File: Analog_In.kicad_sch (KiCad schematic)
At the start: 16 parts, among them J301 Piezos, U301 TL082, U302 TL082, U303 ADS1115IDGS

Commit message: Switch ADC
Switched from the ADS1115 to ADS7924 to get faster sampling time.
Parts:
- removed U303: ADS1115IDGS, Package_SO:TSSOP-10_3x3mm_P0.5mm, symbol Analog_ADC:ADS1115IDGS
- added C305, C306: 1u, Capacitor_SMD:C_0402_1005Metric, symbol Device:C_Small
- added U303: ADS7924, Package_DFN_QFN:WQFN-16-1EP_3x3mm_P0.5mm_EP1.68x1.68mm, symbol Analog_ADC:ADS7924
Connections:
- net +5VA: now also C306.1, U303.15 (AVDD)
- net ADC_AIN0: now also U303.12 (CH0)
- net ADC_AIN1: now also U303.11 (CH1)
- net ADC_AIN2: now also U303.10 (CH2)
- net ADC_AIN3: now also U303.9 (CH3)
- net AIN0: now also J301.2 (Pin_2); no longer J301.8 (Pin_8)
- net AIN1: now also J301.4 (Pin_4); no longer J301.6 (Pin_6)
- net AIN2: now also J301.6 (Pin_6); no longer J301.4 (Pin_4)
- net AIN3: now also J301.8 (Pin_8); no longer J301.2 (Pin_2)
- net GND: now also C305.2, C306.2, U303.17 (pad), U303.5 (A0), U303.6 (DGND), U303.8 (AGND)
- net MCU_ADC_INT: now also U303.2 (~{INT})
- net MCU_SCL: now also U303.3 (SCLK)
- net MCU_SDA: now also U303.4 (SDA)
- new net: U303.13 (MUXOUT), U303.14 (ADCIN)
- new net +3.3V: C305.1, U303.16 (DVDD)
- no-connect marks 0 -> 2

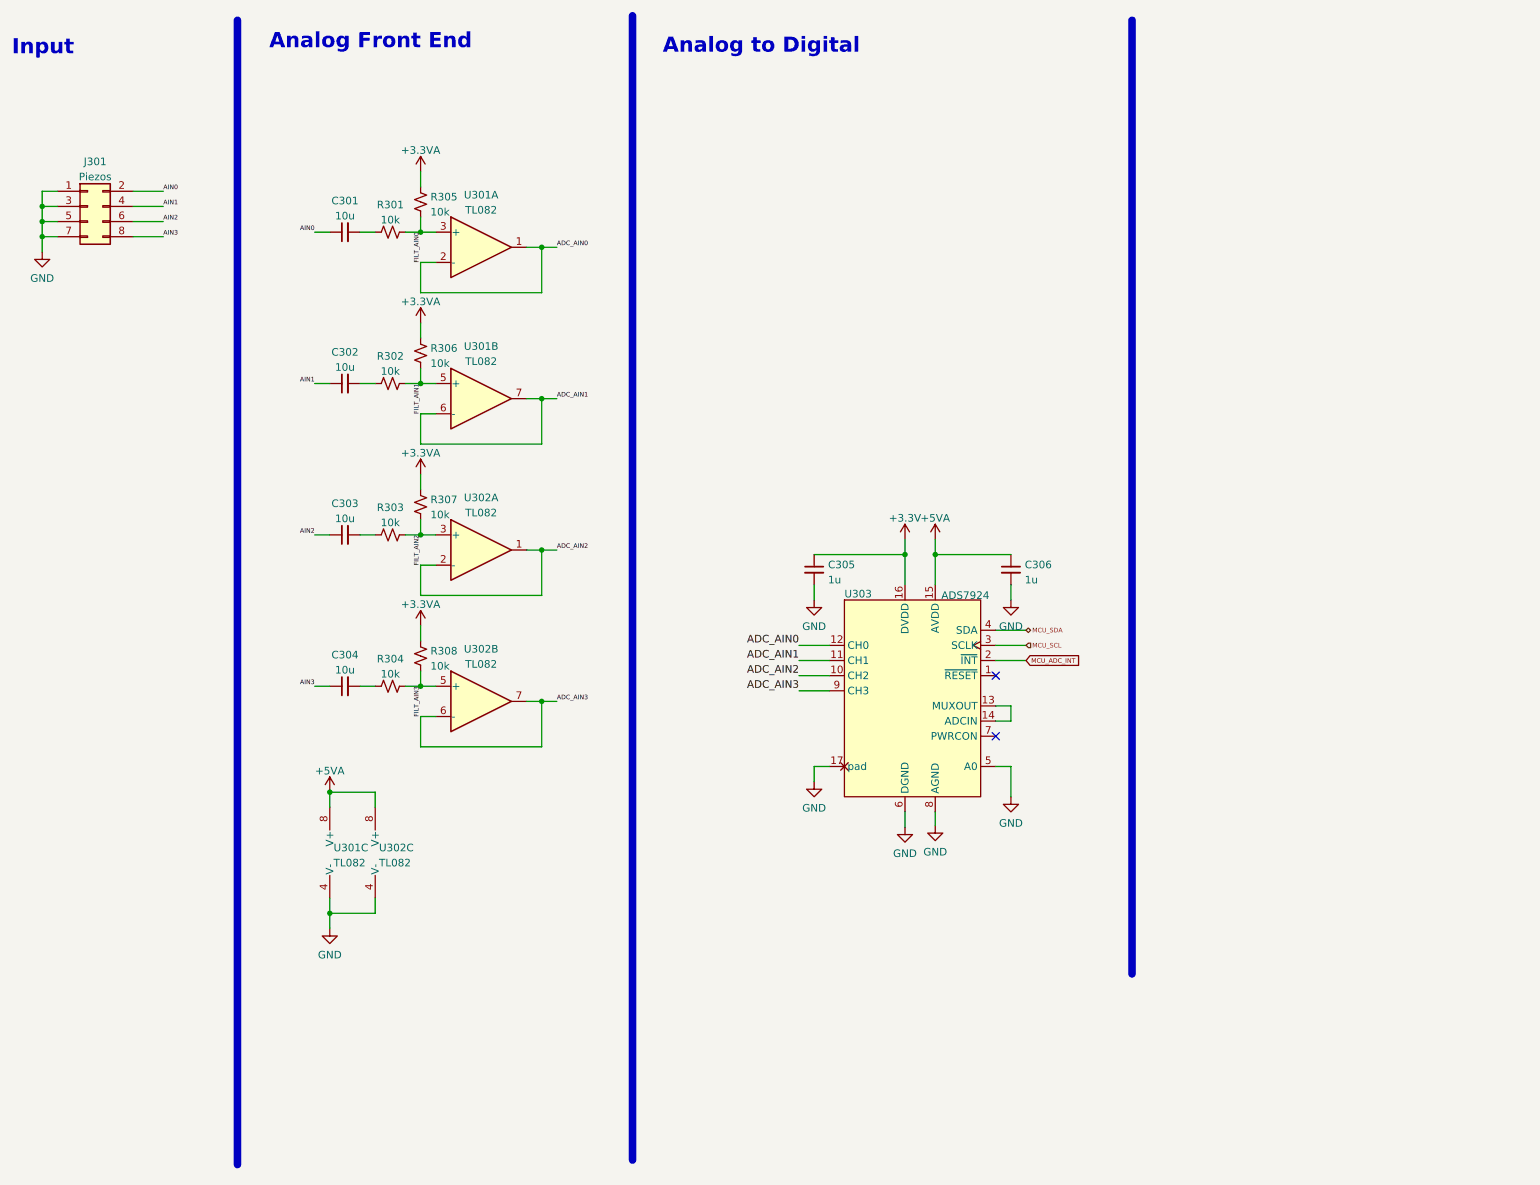
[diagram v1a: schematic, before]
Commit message: Improvements
Switched ADC to ADC128S.
Upgraded USB to USB-C
Improved Analog front end to work with signals better.
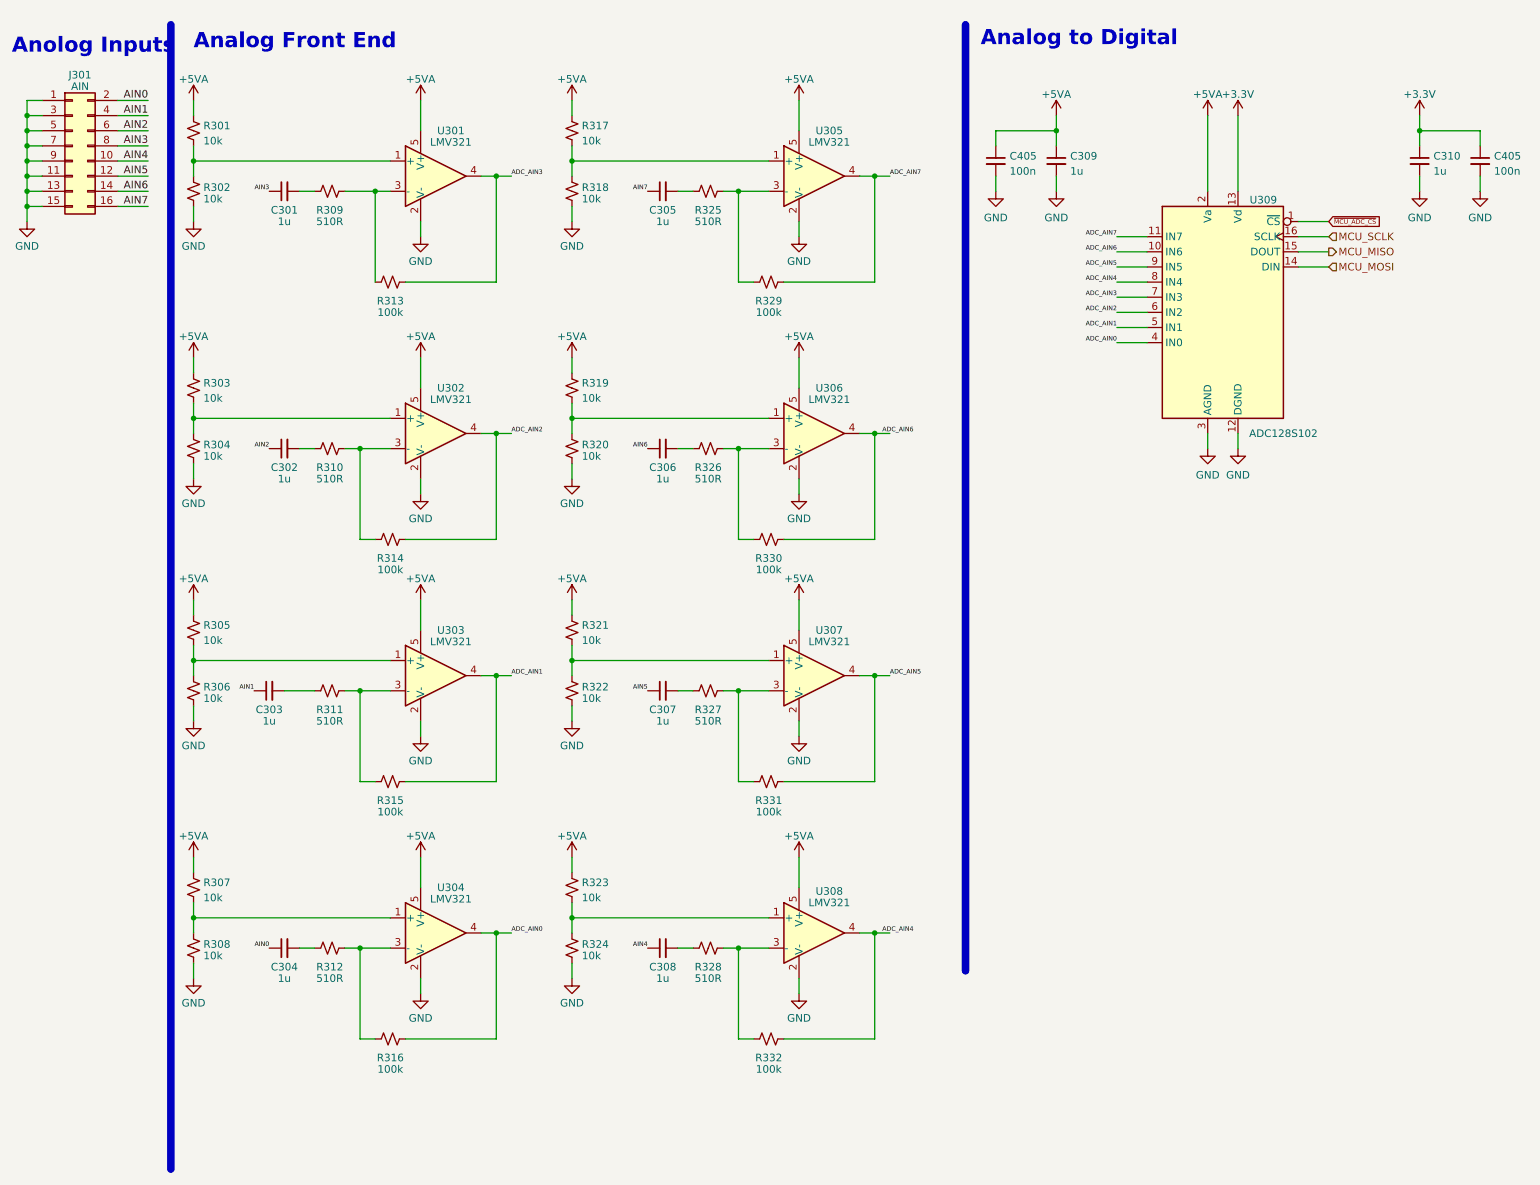
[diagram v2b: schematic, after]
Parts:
- removed J301: Piezos, Connector_PinSocket_2.54mm:PinSocket_2x04_P2.54mm_Vertical, symbol Connector_Generic:Conn_02x04_Odd_Even
- removed U301, U302: TL082, Package_SO:SOIC-8_3.9x4.9mm_P1.27mm, symbol Amplifier_Operational:TL082
- removed U303: ADS7924, Package_DFN_QFN:WQFN-16-1EP_3x3mm_P0.5mm_EP1.68x1.68mm, symbol Analog_ADC:ADS7924
- added C305, C306, C307, C308: 1u, Capacitor_SMD:C_0402_1005Metric, symbol Device:C_Small
- added C405 (x2): 100n, Capacitor_SMD:C_0402_1005Metric, symbol Device:C_Small
- added J301: AIN, Connector_PinHeader_2.54mm:PinHeader_2x08_P2.54mm_Vertical, symbol Connector_Generic:Conn_02x08_Odd_Even
- added R309, R310, R311, R312, R325, R326, R327, R328: 510R, Resistor_SMD:R_0402_1005Metric, symbol Device:R_Small_US
- added R313, R314, R315, R316, R329, R330, R331, R332: 100k, Resistor_SMD:R_0402_1005Metric, symbol Device:R_Small_US
- added R317, R318, R319, R320, R321, R322, R323, R324: 10k, Resistor_SMD:R_0402_1005Metric, symbol Device:R_Small_US
- added U301, U302, U303, U304, U305, U306, U307, U308: LMV321, Package_TO_SOT_SMD:SOT-23-5, symbol Amplifier_Operational:LMV321
- added U309: ADC128S102, Package_SO:TSSOP-16_4.4x5mm_P0.65mm, symbol PickupMic_DSP:ADC128S102
- C301, C302, C303, C304: value 10u -> 1u; footprint Capacitor_SMD:C_0603_1608Metric -> Capacitor_SMD:C_0402_1005Metric; LCSC C19702 -> C52923
- R301: renamed from R305; footprint Resistor_SMD:R_0603_1608Metric -> Resistor_SMD:R_0402_1005Metric; LCSC C25804 -> C144807
- R302: renamed from R301; footprint Resistor_SMD:R_0603_1608Metric -> Resistor_SMD:R_0402_1005Metric; LCSC C25804 -> C144807
- R303: renamed from R306; footprint Resistor_SMD:R_0603_1608Metric -> Resistor_SMD:R_0402_1005Metric; LCSC C25804 -> C144807
- R304: renamed from R302; footprint Resistor_SMD:R_0603_1608Metric -> Resistor_SMD:R_0402_1005Metric; LCSC C25804 -> C144807
- R305: renamed from R307; footprint Resistor_SMD:R_0603_1608Metric -> Resistor_SMD:R_0402_1005Metric; LCSC C25804 -> C144807
- R306: renamed from R303; footprint Resistor_SMD:R_0603_1608Metric -> Resistor_SMD:R_0402_1005Metric; LCSC C25804 -> C144807
- R307: renamed from R308; footprint Resistor_SMD:R_0603_1608Metric -> Resistor_SMD:R_0402_1005Metric; LCSC C25804 -> C144807
- R308: renamed from R304; footprint Resistor_SMD:R_0603_1608Metric -> Resistor_SMD:R_0402_1005Metric; LCSC C25804 -> C144807
- renumbered C305 to C309, C306 to C310
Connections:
- net +3.3VA is gone; now on net +5VA: R301.1, R303.1, R305.1, R307.1
- net +3.3V: now also C310.1, C405.1, U309.13 (Vd); no longer C309.1
- net +5VA: now also C309.1, C405.1, R317.1, R319.1, R321.1, R323.1, U301.5 (V+), U302.5 (V+), U303.5 (V+), U304.5 (V+), U305.5 (V+), U306.5 (V+), U307.5 (V+), U308.5 (V+), U309.2 (Va); no longer C310.1
- net ADC_AIN0: now also R316.2, U304.4, U309.4 (IN0)
- net ADC_AIN1: now also R315.2, U303.4, U309.5 (IN1)
- net ADC_AIN2: now also R314.2, U302.4, U309.6 (IN2)
- net ADC_AIN3: now also R313.2, U301.4, U309.7 (IN3)
- net AIN0: now also C304.1, J301.2 (Pin_2); no longer C301.1
- net AIN1: now also C303.1, J301.4 (Pin_4); no longer C302.1
- net AIN2: now also C302.1, J301.6 (Pin_6); no longer C303.1
- net AIN3: now also C301.1, J301.8 (Pin_8); no longer C304.1
- net GND: now also R302.1, R304.2, R306.1, R308.1, C405.2, C405.2, J301.1 (Pin_1), J301.11 (Pin_11), J301.13 (Pin_13), J301.15 (Pin_15), J301.3 (Pin_3), J301.5 (Pin_5), J301.7 (Pin_7), J301.9 (Pin_9), R318.1, R320.1, R322.1, R324.1, U301.2 (V-), U302.2 (V-), U303.2 (V-), U304.2 (V-), U305.2 (V-), U306.2 (V-), U307.2 (V-), U308.2 (V-), U309.12 (DGND), U309.3 (AGND)
- net at C303.2: now also R311.2; no longer R306.1
- net at C304.2: now also R312.2; no longer R308.1
- net at C301.2: now also R309.2; no longer R302.1
- net at R304.1: now also R303.2, U302.1 (+); no longer C302.2
- net FILT_AIN0: no longer names the net of R301.2, R302.2
- net FILT_AIN0: now also U301.1 (+)
- removed net FILT_AIN1: R303.2, R304.2
- net FILT_AIN2: no longer names the net of R305.2, R306.2
- net FILT_AIN2: now also U303.1 (+)
- net FILT_AIN3: no longer names the net of R307.2, R308.2
- net FILT_AIN3: now also U304.1 (+)
- new net: R321.2, R322.2, U307.1 (+)
- new net: R317.2, R318.2, U305.1 (+)
- new net: R325.1, R329.1, U305.3 (-)
- new net: C307.2, R327.2
- new net: R309.1, R313.1, U301.3 (-)
- new net: C305.2, R325.2
- new net: R327.1, R331.1, U307.3 (-)
- new net: C306.2, R326.2
- new net: R323.2, R324.2, U308.1 (+)
- new net: R310.1, R314.1, U302.3 (-)
- new net: R328.1, R332.1, U308.3 (-)
- new net: C308.2, R328.2
- new net: C302.2, R310.2
- new net: R326.1, R330.1, U306.3 (-)
- new net: R319.2, R320.2, U306.1 (+)
- new net: R312.1, R316.1, U304.3 (-)
- new net: R311.1, R315.1, U303.3 (-)
- new net ADC_AIN4: R332.2, U308.4, U309.8 (IN4)
- new net ADC_AIN5: R331.2, U307.4, U309.9 (IN5)
- new net ADC_AIN6: R330.2, U306.4, U309.10 (IN6)
- new net ADC_AIN7: R329.2, U305.4, U309.11 (IN7)
- new net AIN4: C308.1, J301.10 (Pin_10)
- new net AIN5: C307.1, J301.12 (Pin_12)
- new net AIN6: C306.1, J301.14 (Pin_14)
- new net AIN7: C305.1, J301.16 (Pin_16)
- new net MCU_MISO: U309.15 (DOUT)
- new net MCU_MOSI: U309.14 (DIN)
- new net MCU_SCLK: U309.16 (SCLK)
- new net ~{MCU_ADC_CS}: U309.1 (~{CS})
- no-connect marks 2 -> 0
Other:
- note added: "Anolog Inputs"
- note removed: "Input"
- moved on the sheet: C309, C310, R301, R302, R303, R304, R305, R306, R307, R308
